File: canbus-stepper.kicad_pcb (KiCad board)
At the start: 2 copper layers, 40.3 x 40.3 mm, 57 parts, among them J1 TYPE-C USB SOCKET, J2 Motor Output, J3 CAN Daisy-Chain 1, J4 CAN Daisy-Chain 2, J5 Qwiic I2C, J6 AUX Port, J7 SFV30R-2STBE1HLF (30-Pin OLED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, J8 24V Power Input Terminal, J9 24V Power Output Terminal, SW1 SW_Push, SW2 SW_Push, SW3 SW_Push, SW4 SW_Push, U1 ESP32-S3-WROOM-1, U2 TMC2209, U3 MT6701, U4 SN65HVD230, U5 MP2315, U6 AP2112K-3.3TRG1

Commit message: Updated SW1-SW4, U6, J2 footprints & values in both schematic and PCB files
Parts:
- C10: footprint Capacitor_SMD:C_0805_2012Metric -> CANBUS-Stepper:JST_S4B-PH-SM4-TB
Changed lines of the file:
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@@
 		)
 	)
-	(footprint "Capacitor_SMD:C_0805_2012Metric"
+	(footprint "CANBUS-Stepper:JST_S4B-PH-SM4-TB"
 		(layer "F.Cu")
 		(at 203.625 120.785)
@@
 		)
 		(embedded_fonts no)
-		(model "${KICAD10_3DMODEL_DIR}/Capacitor_SMD.3dshapes/C_0805_2012Metric.step"
+		(model "${KIPRJMOD}/3dmodels/S4B-PH-SM4-TB.step"
 			(offset
 				(xyz 0 0 0)

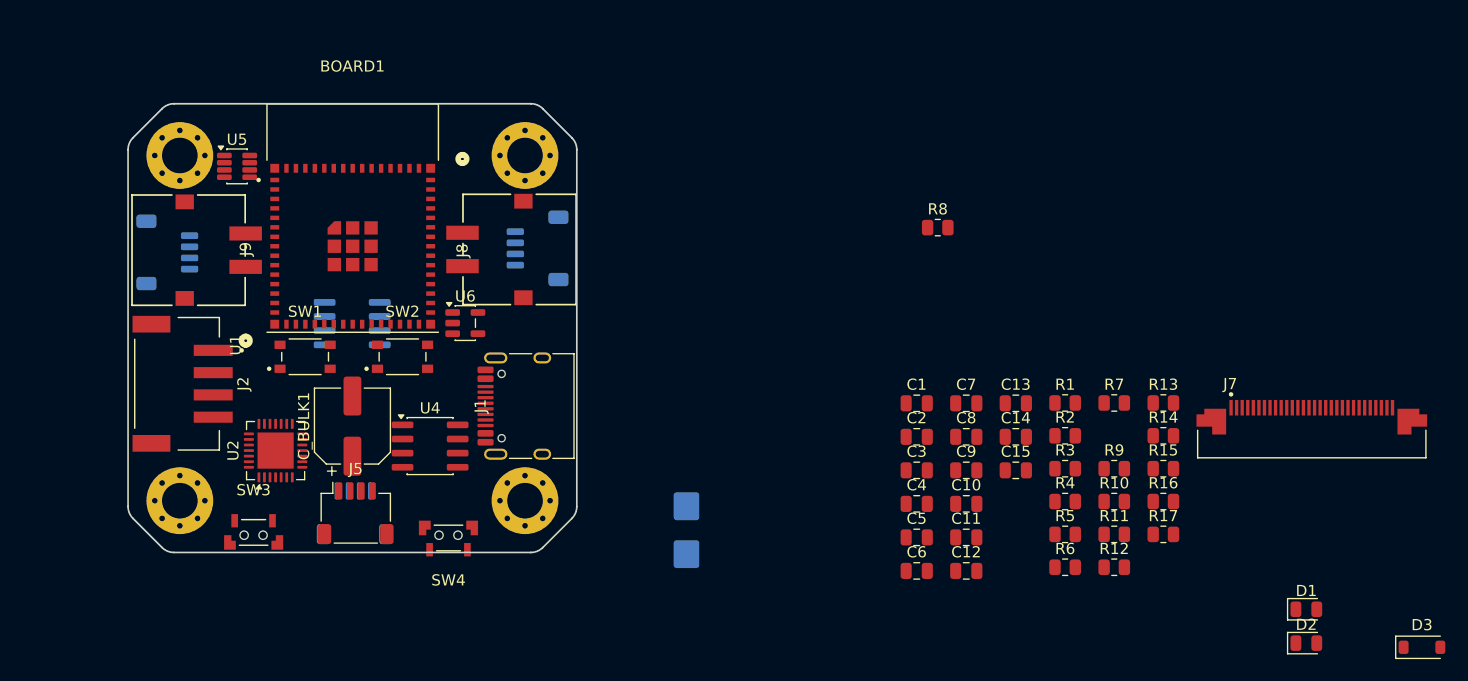
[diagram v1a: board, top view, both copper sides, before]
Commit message: feat: complete hardware schematic fixes, 0603 footprint optimizations, AS5600 encoder, TCAN1051V transceiver, and IPC-2221 design rules
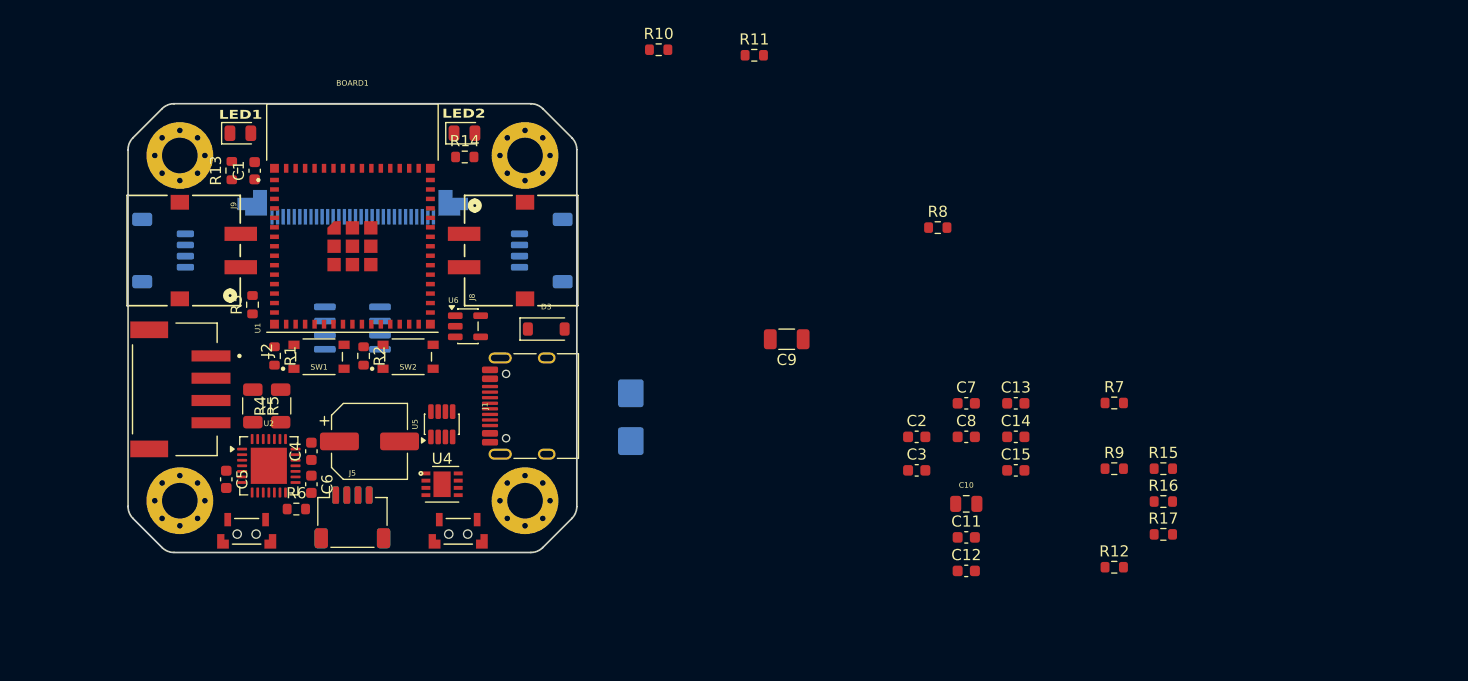
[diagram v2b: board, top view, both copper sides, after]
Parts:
- C1, C11, C12, C13, C14, C15, C2, C3, C4, C5, C6, C7, C8: footprint Capacitor_SMD:C_0805_2012Metric -> Capacitor_SMD:C_0603_1608Metric
- C10: footprint CANBUS-Stepper:JST_S4B-PH-SM4-TB -> Capacitor_SMD:C_0805_2012Metric
- C9: footprint Capacitor_SMD:C_0805_2012Metric -> Capacitor_SMD:C_1206_3216Metric
- J7: moved to B.Cu
- R1, R10, R11, R12, R13, R14, R15, R16, R17, R2, R3, R6, R7, R8, R9: footprint Resistor_SMD:R_0805_2012Metric -> Resistor_SMD:R_0603_1608Metric
- R4, R5: footprint Resistor_SMD:R_0805_2012Metric -> Resistor_SMD:R_1206_3216Metric
- U3: value MT6701 -> AS5600-ASOT
- U4: value SN65HVD230 -> TCAN1051VDRBTQ1; footprint Package_SO:SOIC-8_3.9x4.9mm_P1.27mm -> CANBUS-Stepper:TCAN1051VDRBTQ1
- moved D1 104.8 mm to (138.4, 87.5)
- moved D2 88.4 mm to (158.6, 87.5)
- moved J7 87.8 mm to (148.5, 95.0)
- moved R13 86.2 mm to (137.7, 90.9), turned to 90 degrees
- moved D3 83.7 mm to (165.9, 105.1)
- moved R3 74.5 mm to (139.5, 102.9), turned to 90 degrees
- moved R5 73.9 mm to (139.6, 112.0), turned to -90 degrees
- moved R1 71.1 mm to (141.5, 107.5), turned to -90 degrees
- moved R4 71.0 mm to (142.1, 112.0), turned to 90 degrees
- moved R6 69.2 mm to (143.5, 121.2)
- moved R14 67.6 mm to (158.6, 89.6)
- moved R2 63.4 mm to (149.5, 107.5), turned to -90 degrees
- moved C1 63.0 mm to (139.7, 90.9), turned to 90 degrees
- moved C5 62.2 mm to (137.2, 118.6), turned to -90 degrees
- moved R10 57.6 mm to (176.0, 80.0)
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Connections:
- SW1 pad 1: /SW1 -> /EN
- SW2 pad 1: /SW2 -> /IO0
- SW3 pad 1: /EN -> /SW1
- SW4 pad 1: /IO0 -> /SW2
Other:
- board text added: "LED1"
- board text added: "LED2"

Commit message: feat: update schematic and pcb layout design files
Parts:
- moved TVS1 51.2 mm to (124.5, 98.0)

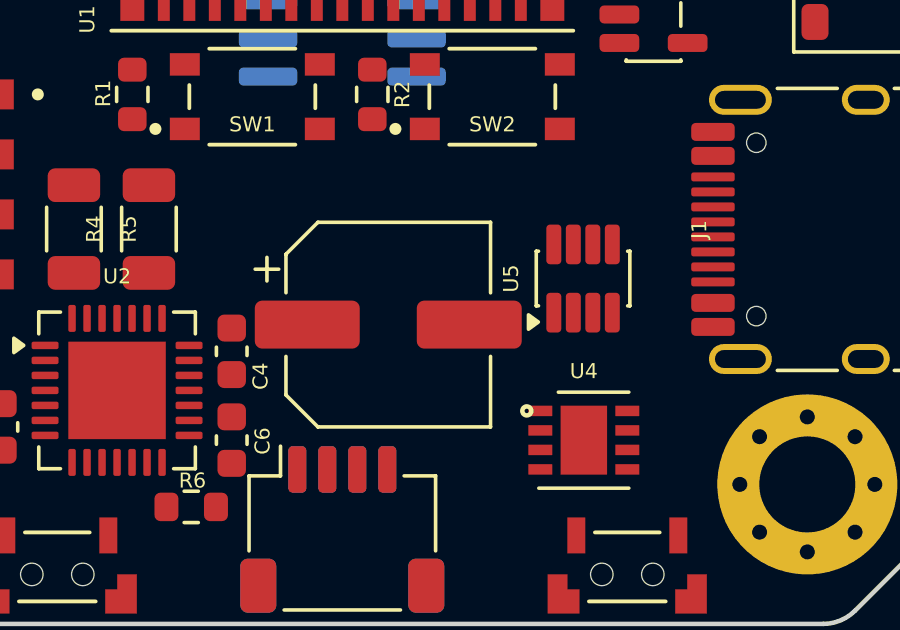
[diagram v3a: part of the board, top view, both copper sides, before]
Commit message: feat: set exact datasheet values for all passive resistors (R1-R17) and capacitors (C1-C15)
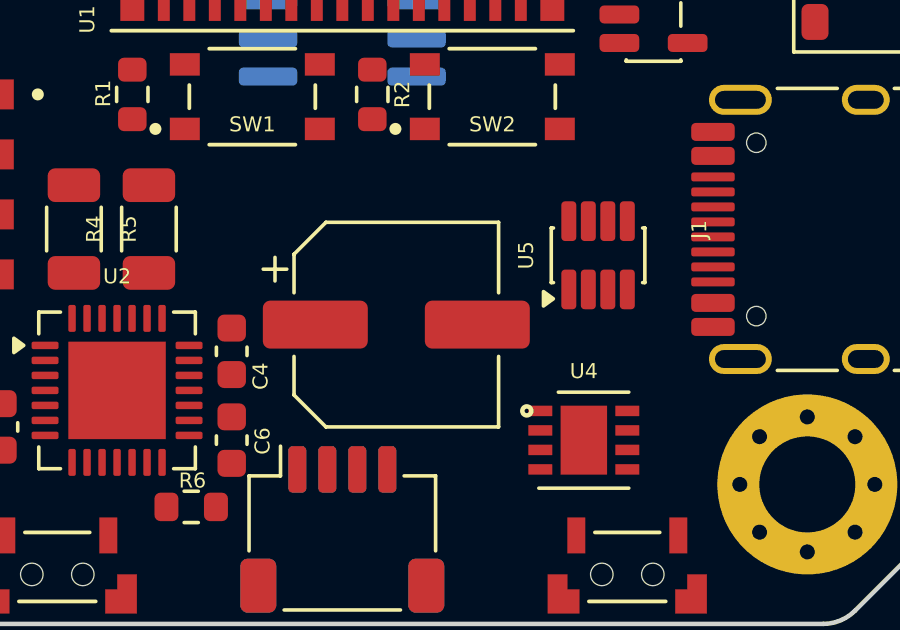
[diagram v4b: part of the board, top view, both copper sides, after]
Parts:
- C1: value C1 -> 1uF
- C10: value C10 -> 22uF
- C11: value C11 -> 1uF
- C12: value C12 -> 1uF
- C13: value C13 -> 1uF
- C14: value C14 -> 4.7uF
- C15: value C15 -> 4.7uF
- C2: value C2 -> 100nF
- C3: value C3 -> 100nF 50V
- C4: value C4 -> 100nF 50V
- C5: value C5 -> 22nF 50V
- C6: value C6 -> 100nF
- C7: value C7 -> 100nF
- C8: value C8 -> 100nF
- C9: value C9 -> 10uF 50V
- R1: value R1 -> 10k
- R10: value R10 -> 100k
- R11: value R11 -> 10k
- R12: value R12 -> 10k
- R13: value R13 -> 1k
- R14: value R14 -> 1k
- R15: value R15 -> 5.1k
- R16: value R16 -> 5.1k
- R17: value R17 -> 390k
- R2: value R2 -> 10k
- R3: value R3 -> 10k
- R4: value R4 -> 0.11R
- R5: value R5 -> 0.11R
- R6: value R6 -> 1k
- R7: value R7 -> 4.7k
- R8: value R8 -> 4.7k
- R9: value R9 -> 120R
- moved U5 0.92 mm to (157.0, 112.9)
- moved C_BULK1 0.27 mm to (150.3, 115.2)
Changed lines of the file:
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@@
 			)
 		)
-		(property "Value" "C10"
+		(property "Value" "22uF"
 			(at 0 1.68 0)
 			(layer "F.Fab")
@@
 			)
 		)
-		(property "Value" "R15"
+		(property "Value" "5.1k"
 			(at 0 1.43 0)
 			(layer "F.Fab")
@@
 			)
 		)
-		(property "Value" "C15"
+		(property "Value" "4.7uF"
 			(at 0 1.43 0)
 			(layer "F.Fab")
@@
 			)
 		)
-		(property "Value" "R16"
+		(property "Value" "5.1k"
 			(at 0 1.43 0)
 			(layer "F.Fab")
@@
 			)
 		)
-		(property "Value" "R6"
+		(property "Value" "1k"
 			(at 0 1.43 0)
 			(layer "F.Fab")
@@
 			)
 		)
-		(property "Value" "C2"
+		(property "Value" "100nF"
 			(at 0 1.43 0)
 			(layer "F.Fab")
@@
 			)
 		)
-		(property "Value" "R17"
+		(property "Value" "390k"
 			(at 0 1.43 0)
 			(layer "F.Fab")
@@
 			)
 		)
-		(property "Value" "R13"
+		(property "Value" "1k"
 			(at 0 1.43 90)
 			(layer "F.Fab")
@@
 			)
 		)
-		(property "Value" "C8"
+		(property "Value" "100nF"
 			(at 0 1.43 0)
 			(layer "F.Fab")
@@
 			)
 		)
-		(property "Value" "R2"
+		(property "Value" "10k"
 			(at 0 1.43 270)
 			(layer "F.Fab")
@@
 	(footprint "Package_TO_SOT_SMD:SOT-23-8"
 		(layer "F.Cu")
-		(at 156.525 113.6375 90)
+		(at 157.025 112.8625 90)
 		(descr "SOT, 8 Pin (JEDEC MO-178 Var BA https://www.jedec.org/document_search?search_api_views_fulltext=MO-178)")
 		(tags "SOT TO_SOT_SMD")
@@
 			)
 		)
-		(property "Value" "C13"
+		(property "Value" "1uF"
 			(at 0 1.43 0)
 			(layer "F.Fab")
@@
 			)
 		)
-		(property "Value" "R4"
+		(property "Value" "0.11R"
 			(at 0 1.83 90)
 			(layer "F.Fab")
@@
 	(footprint "Capacitor_SMD:CP_Elec_6.3x5.8"
 		(layer "F.Cu")
-		(at 150.031678 115.173177)
+		(at 150.3 115.173177)
 		(descr "SMD capacitor, aluminum electrolytic, Nichicon, 6.3x5.8mm")
 		(tags "capacitor electrolytic")
@@
 			)
 		)
-		(property "Value" "R10"
+		(property "Value" "100k"
 			(at 0 1.43 0)
 			(layer "F.Fab")
@@
 			)
 		)
-		(property "Value" "C14"
+		(property "Value" "4.7uF"
 			(at 0 1.43 0)
 			(layer "F.Fab")
@@
 			)
 		)
-		(property "Value" "R12"
+		(property "Value" "10k"
 			(at 0 1.43 0)
 			(layer "F.Fab")
@@
 			)
 		)
-		(property "Value" "R14"
+		(property "Value" "1k"
 			(at 0 1.43 0)
 			(layer "F.Fab")
@@
 			)
 		)
-		(property "Value" "C3"
+		(property "Value" "100nF 50V"
 			(at 0 1.43 0)
 			(layer "F.Fab")
@@
 			)
 		)
-		(property "Value" "C4"
+		(property "Value" "100nF 50V"
 			(at 0 1.43 90)
 			(layer "F.Fab")
@@
 			)
 		)
-		(property "Value" "C9"
+		(property "Value" "10uF 50V"
 			(at 0 1.85 180)
 			(layer "F.Fab")
@@
 			)
 		)
-		(property "Value" "R9"
+		(property "Value" "120R"
 			(at 0 1.43 0)
 			(layer "F.Fab")
@@
 			)
 		)
-		(property "Value" "R5"
+		(property "Value" "0.11R"
 			(at 0 1.83 270)
 			(layer "F.Fab")
@@
 			)
 		)
-		(property "Value" "C11"
+		(property "Value" "1uF"
 			(at 0 1.43 0)
 			(layer "F.Fab")
@@
 			)
 		)
-		(property "Value" "C1"
+		(property "Value" "1uF"
 			(at 0 1.43 90)
 			(layer "F.Fab")
@@
 			)
 		)
-		(property "Value" "C7"
+		(property "Value" "100nF"
 			(at 0 1.43 0)
 			(layer "F.Fab")
@@
 			)
 		)
-		(property "Value" "R8"
+		(property "Value" "4.7k"
 			(at 0 1.43 0)
 			(layer "F.Fab")
@@
 			)
 		)
-		(property "Value" "R1"
+		(property "Value" "10k"
 			(at 0 1.43 270)
 			(layer "F.Fab")
@@
 			)
 		)
-		(property "Value" "R11"
+		(property "Value" "10k"
 			(at 0 1.43 0)
 			(layer "F.Fab")
@@
 			)
 		)
-		(property "Value" "C6"
+		(property "Value" "100nF"
 			(at 0 1.43 270)
 			(layer "F.Fab")
@@
 			)
 		)
-		(property "Value" "R3"
+		(property "Value" "10k"
 			(at 0 1.43 90)
 			(layer "F.Fab")
@@
 			)
 		)
-		(property "Value" "C5"
+		(property "Value" "22nF 50V"
 			(at 0 1.43 270)
 			(layer "F.Fab")
@@
 			)
 		)
-		(property "Value" "R7"
+		(property "Value" "4.7k"
 			(at 0 1.43 0)
 			(layer "F.Fab")
@@
 			)
 		)
-		(property "Value" "C12"
+		(property "Value" "1uF"
 			(at 0 1.43 0)
 			(layer "F.Fab")

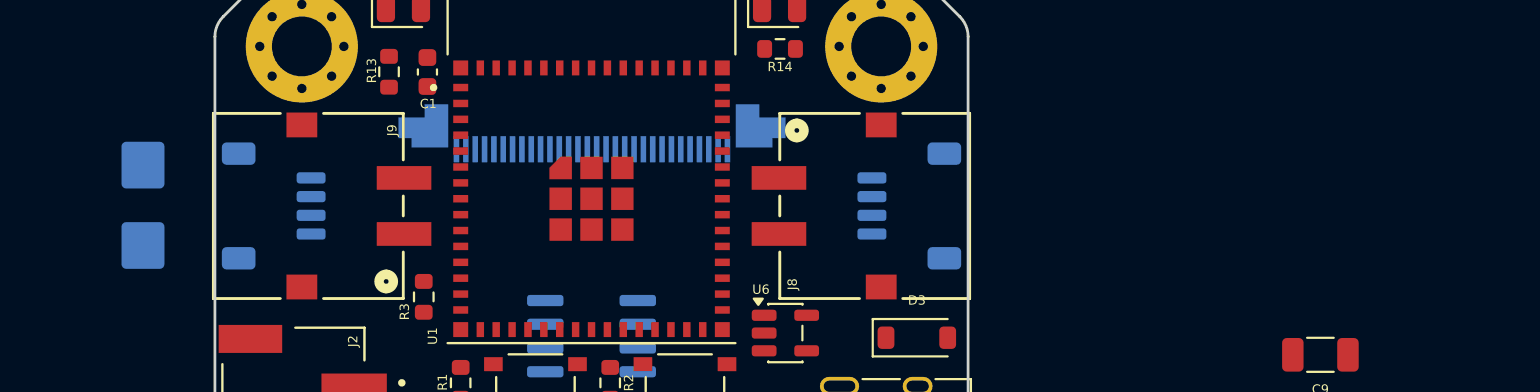
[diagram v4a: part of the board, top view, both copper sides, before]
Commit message: feat: add 24V PPTC fuse, P-FET reverse polarity protection, USB PPTC fuse, CAN TVS, and USB ESD arrays
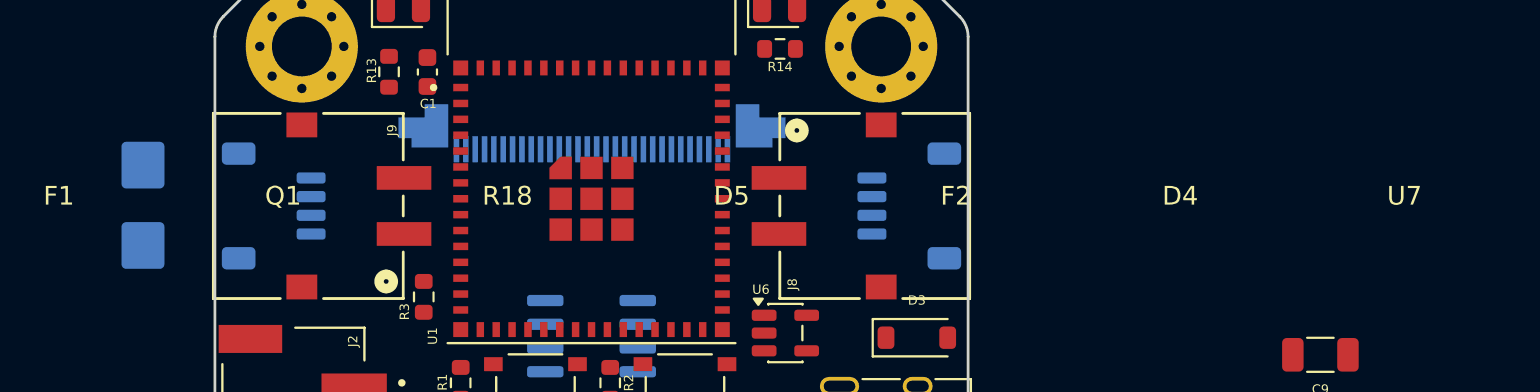
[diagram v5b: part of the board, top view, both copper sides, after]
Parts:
- added D4: PESD1CAN, Package_TO_SOT_SMD:SOT-23, F.Cu at (180.0, 100.0)
- added D5: BZX84C12V, Diode_SMD:D_SOT-23_ANK, F.Cu at (156.0, 100.0)
- added F1: 3.5A 30V PPTC, Fuse:Fuse_1812_4532Metric, F.Cu at (120.0, 100.0)
- added F2: 500mA 16V PPTC, Fuse:Fuse_0805_2012Metric, F.Cu at (168.0, 100.0)
- added Q1: AO4407A, Package_SO:SOIC-8_3.9x4.9mm_P1.27mm, F.Cu at (132.0, 100.0)
- added R18: 10k, Resistor_SMD:R_0603_1608Metric, F.Cu at (144.0, 100.0)
- added U7: USBLC6-2SC6, Package_TO_SOT_SMD:SOT-23-6, F.Cu at (192.0, 100.0)
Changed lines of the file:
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@@
 	)
 	(embedded_fonts no)
+  (footprint "Fuse:Fuse_1812_4532Metric"
+    (layer "F.Cu")
+    (at 120.00 100.00)
+    (property "Reference" "F1"
+      (at 0 -2.5 0)
+      (layer "F.SilkS")
+      (effects
+        (font
+          (size 1 1)
+          (thickness 0.15)
+        )
+      )
+    )
+    (property "Value" "3.5A 30V PPTC"
+      (at 0 2.5 0)
+      (layer "F.Fab")
+      (effects
+        (font
+          (size 1 1)
+          (thickness 0.15)
+        )
+      )
+    )
+  )
+  (footprint "Package_SO:SOIC-8_3.9x4.9mm_P1.27mm"
+    (layer "F.Cu")
+    (at 132.00 100.00)
+    (property "Reference" "Q1"
+      (at 0 -2.5 0)
+      (layer "F.SilkS")
+      (effects
+        (font
+          (size 1 1)
+          (thickness 0.15)
+        )
+      )
+    )
+    (property "Value" "AO4407A"
+      (at 0 2.5 0)
+      (layer "F.Fab")
+      (effects
+        (font
+          (size 1 1)
+          (thickness 0.15)
+        )
+      )
+    )
+  )
+  (footprint "Resistor_SMD:R_0603_1608Metric"
+    (layer "F.Cu")
+    (at 144.00 100.00)
+    (property "Reference" "R18"
+      (at 0 -2.5 0)
+      (layer "F.SilkS")
+      (effects
+        (font
+          (size 1 1)
+          (thickness 0.15)
+        )
+      )
+    )
+    (property "Value" "10k"
+      (at 0 2.5 0)
+      (layer "F.Fab")
+      (effects
+        (font
+          (size 1 1)
+          (thickness 0.15)
+        )
+      )
+    )
+  )
+  (footprint "Diode_SMD:D_SOT-23_ANK"
+    (layer "F.Cu")
+    (at 156.00 100.00)
+    (property "Reference" "D5"
+      (at 0 -2.5 0)
+      (layer "F.SilkS")
+      (effects
+        (font
+          (size 1 1)
+          (thickness 0.15)
+        )
+      )
+    )
+    (property "Value" "BZX84C12V"
+      (at 0 2.5 0)
+      (layer "F.Fab")
+      (effects
+        (font
+          (size 1 1)
+          (thickness 0.15)
+        )
+      )
+    )
+  )
+  (footprint "Fuse:Fuse_0805_2012Metric"
+    (layer "F.Cu")
+    (at 168.00 100.00)
+    (property "Reference" "F2"
+      (at 0 -2.5 0)
+      (layer "F.SilkS")
+      (effects
+        (font
+          (size 1 1)
+          (thickness 0.15)
+        )
+      )
+    )
+    (property "Value" "500mA 16V PPTC"
+      (at 0 2.5 0)
+      (layer "F.Fab")
+      (effects
+        (font
+          (size 1 1)
+          (thickness 0.15)
+        )
+      )
+    )
+  )
+  (footprint "Package_TO_SOT_SMD:SOT-23"
+    (layer "F.Cu")
+    (at 180.00 100.00)
+    (property "Reference" "D4"
+      (at 0 -2.5 0)
+      (layer "F.SilkS")
+      (effects
+        (font
+          (size 1 1)
+          (thickness 0.15)
+        )
+      )
+    )
+    (property "Value" "PESD1CAN"
+      (at 0 2.5 0)
+      (layer "F.Fab")
+      (effects
+        (font
+          (size 1 1)
+          (thickness 0.15)
+        )
+      )
+    )
+  )
+  (footprint "Package_TO_SOT_SMD:SOT-23-6"
+    (layer "F.Cu")
+    (at 192.00 100.00)
+    (property "Reference" "U7"
+      (at 0 -2.5 0)
+      (layer "F.SilkS")
+      (effects
+        (font
+          (size 1 1)
+          (thickness 0.15)
+        )
+      )
+    )
+    (property "Value" "USBLC6-2SC6"
+      (at 0 2.5 0)
+      (layer "F.Fab")
+      (effects
+        (font
+          (size 1 1)
+          (thickness 0.15)
+        )
+      )
+    )
+  )
 )
